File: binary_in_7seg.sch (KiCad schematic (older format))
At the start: 9 parts

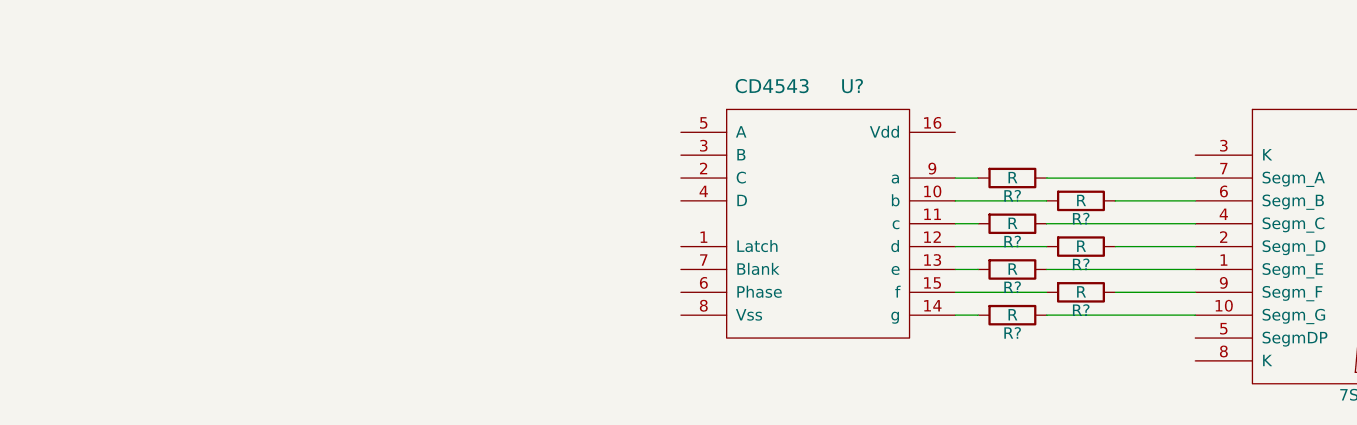
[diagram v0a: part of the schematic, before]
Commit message: Filled in more of the schematic
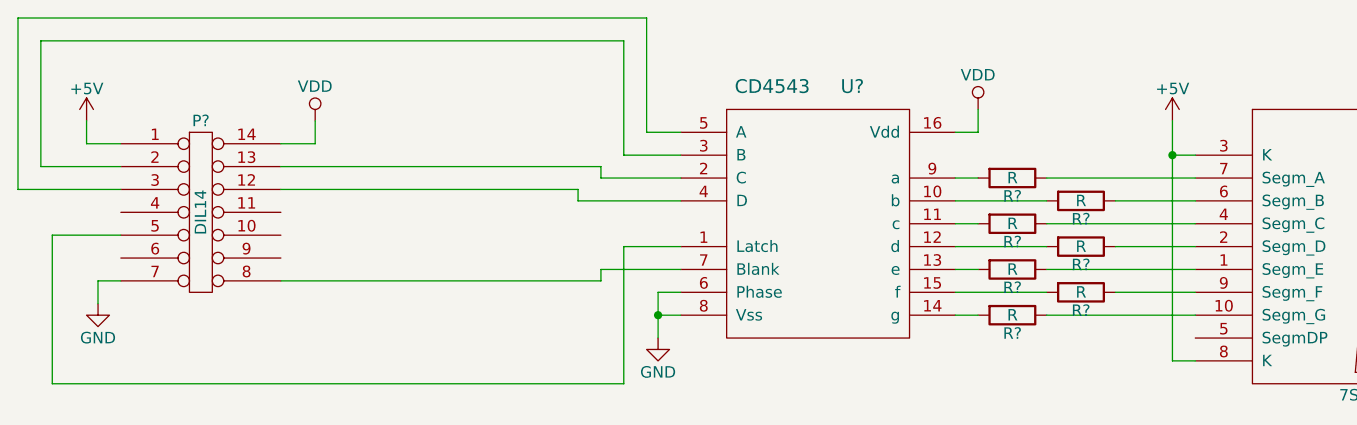
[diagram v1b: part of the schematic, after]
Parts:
- added P?: DIL14, symbol DIL14
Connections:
- net +5V: now reaches S?.3 (K)
- net +5V: now also S?.8 (K), P?.1
- net at U?.1 (Latch): now also P?.5
- net VDD: now reaches U?.16 (Vdd)
- net VDD: now also P?.14
- net at U?.2 (C): now also P?.13
- net at U?.3 (B): now also P?.2
- net at U?.4 (D): now also P?.12
- net at U?.5 (A): now also P?.3
- net GND: now reaches U?.6 (Phase)
- net GND: now also U?.8 (Vss), P?.7
- net at U?.7 (Blank): now also P?.8

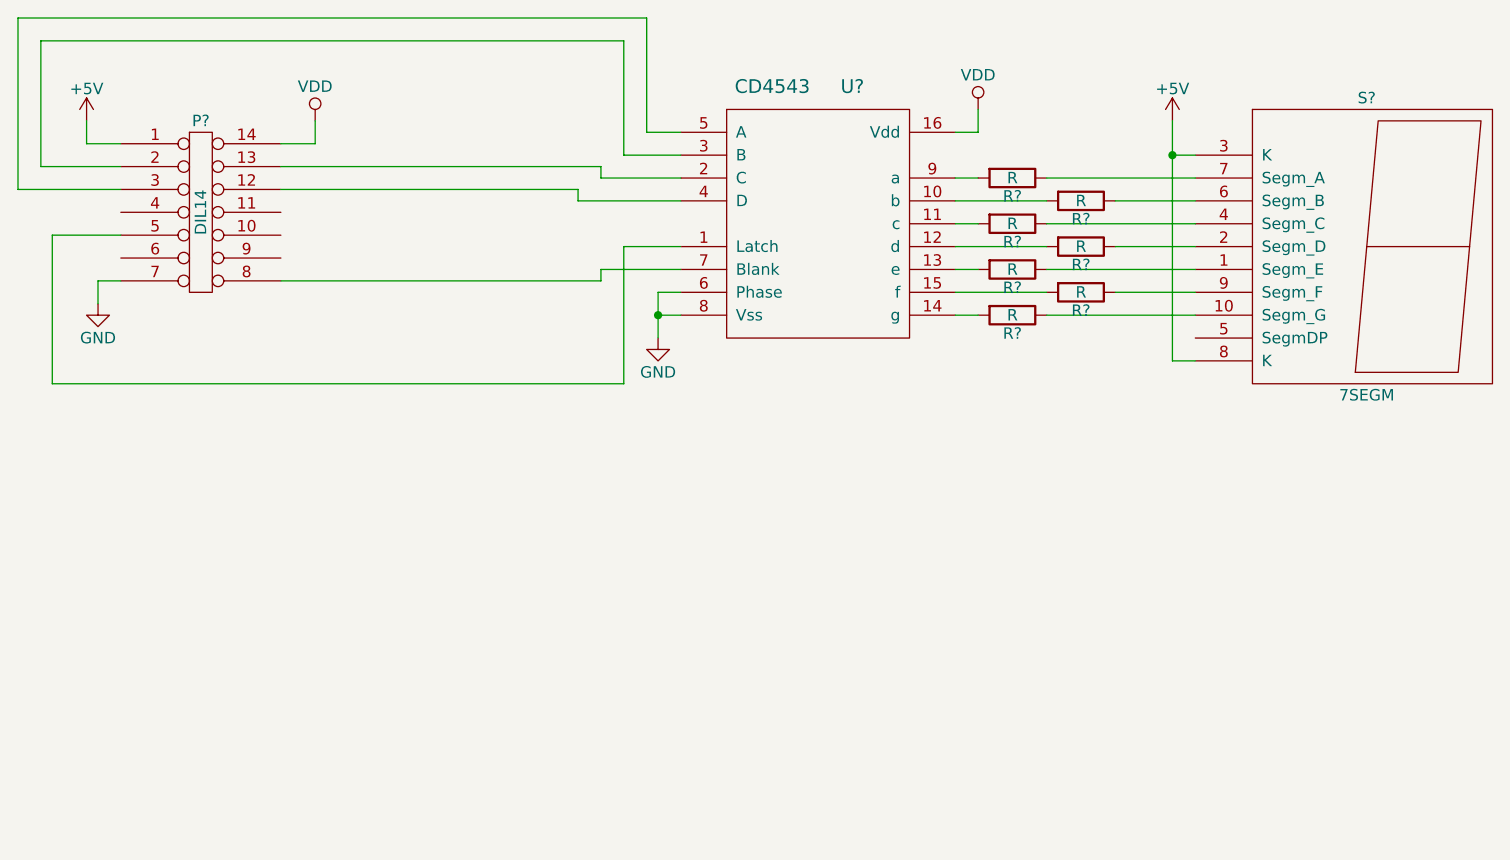
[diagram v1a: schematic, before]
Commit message: Added decimal point input
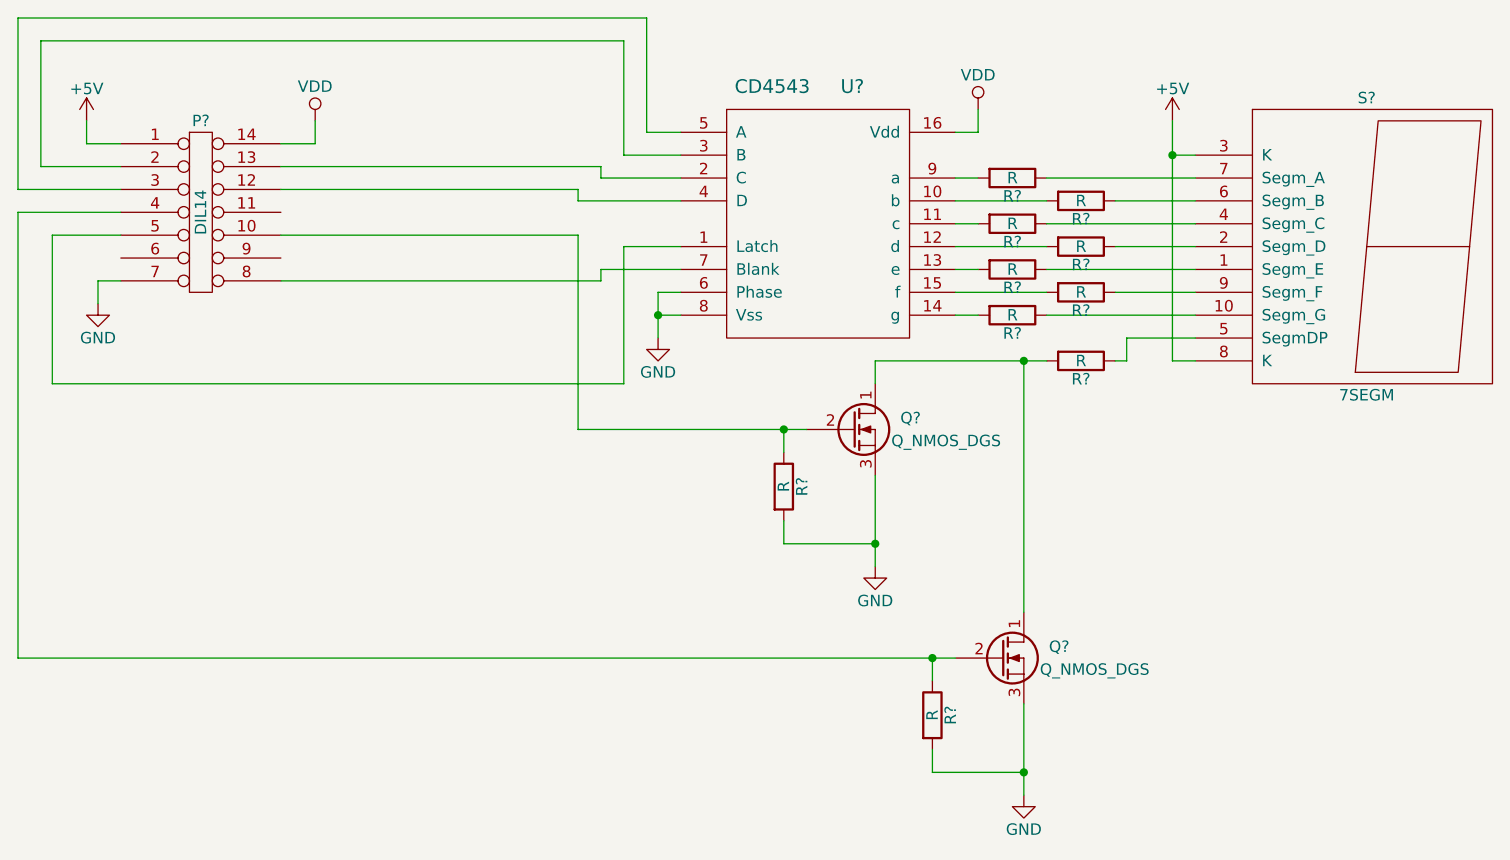
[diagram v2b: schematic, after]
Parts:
- added Q? (x2): Q_NMOS_DGS, symbol Q_NMOS_DGS
- added R? (x3): R, symbol R
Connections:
- net GND: now also Q?.3 (S), Q?.3 (S), R?.2, R?.2
- net at S?.5 (SegmDP): now also R?.1
- net at P?.10: now also Q?.2 (G), R?.1
- net at P?.4: now also Q?.2 (G), R?.1
- new net: Q?.1 (D), Q?.1 (D), R?.2
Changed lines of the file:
@@
 $EndComp
 Wire Wire Line
-	8200 2650 8200 3700
+	8200 2650 8200 2800
+Wire Wire Line
+	8200 2800 8200 3700
 Wire Wire Line
 	8200 2800 8300 2800
@@
 $EndComp
 Wire Wire Line
-	5950 3400 5950 3600
+	5950 3400 5950 3500
+Wire Wire Line
+	5950 3500 5950 3600
 Wire Wire Line
 	5950 3500 6050 3500
@@
 	6050 3400 5950 3400
 Connection ~ 5950 3500
+$Comp
+L Q_NMOS_DGS Q?
+U 1 1 57E026D3
+P 6800 4000
+F 0 "Q?" H 7100 4050 50  0000 R CNN
+F 1 "Q_NMOS_DGS" H 7450 3950 50  0000 R CNN
+F 2 "" H 7000 4100 50  0000 C CNN
+F 3 "" H 6800 4000 50  0000 C CNN
+	1    6800 4000
+	1    0    0    -1
+$EndComp
+$Comp
+L Q_NMOS_DGS Q?
+U 1 1 57E0271C
+P 7450 5000
+F 0 "Q?" H 7750 5050 50  0000 R CNN
+F 1 "Q_NMOS_DGS" H 8100 4950 50  0000 R CNN
+F 2 "" H 7650 5100 50  0000 C CNN
+F 3 "" H 7450 5000 50  0000 C CNN
+	1    7450 5000
+	1    0    0    -1
+$EndComp
+$Comp
+L GND #PWR?
+U 1 1 57E027E1
+P 6900 4600
+F 0 "#PWR?" H 6900 4350 50  0001 C CNN
+F 1 "GND" H 6900 4450 50  0000 C CNN
+F 2 "" H 6900 4600 50  0000 C CNN
+F 3 "" H 6900 4600 50  0000 C CNN
+	1    6900 4600
+	1    0    0    -1
+$EndComp
+$Comp
+L GND #PWR?
+U 1 1 57E0284C
+P 7550 5600
+F 0 "#PWR?" H 7550 5350 50  0001 C CNN
+F 1 "GND" H 7550 5450 50  0000 C CNN
+F 2 "" H 7550 5600 50  0000 C CNN
+F 3 "" H 7550 5600 50  0000 C CNN
+	1    7550 5600
+	1    0    0    -1
+$EndComp
+Wire Wire Line
+	7550 5200 7550 5500
+Wire Wire Line
+	7550 5500 7550 5600
+Wire Wire Line
+	6900 4200 6900 4500
+Wire Wire Line
+	6900 4500 6900 4600
+$Comp
+L R R?
+U 1 1 57E02906
+P 6500 4250
+F 0 "R?" V 6580 4250 50  0000 C CNN
+F 1 "R" V 6500 4250 50  0000 C CNN
+F 2 "" V 6430 4250 50  0000 C CNN
+F 3 "" H 6500 4250 50  0000 C CNN
+	1    6500 4250
+	1    0    0    -1
+$EndComp
+$Comp
+L R R?
+U 1 1 57E02947
+P 7150 5250
+F 0 "R?" V 7230 5250 50  0000 C CNN
+F 1 "R" V 7150 5250 50  0000 C CNN
+F 2 "" V 7080 5250 50  0000 C CNN
+F 3 "" H 7150 5250 50  0000 C CNN
+	1    7150 5250
+	1    0    0    -1
+$EndComp
+Wire Wire Line
+	6500 4100 6500 4000
+Wire Wire Line
+	5600 4000 6500 4000
+Wire Wire Line
+	6500 4000 6600 4000
+Wire Wire Line
+	7150 5100 7150 5000
+Wire Wire Line
+	3150 5000 7150 5000
+Wire Wire Line
+	7150 5000 7250 5000
+Wire Wire Line
+	7150 5400 7150 5500
+Wire Wire Line
+	7150 5500 7550 5500
+Connection ~ 7550 5500
+Wire Wire Line
+	6500 4400 6500 4500
+Wire Wire Line
+	6500 4500 6900 4500
+Connection ~ 6900 4500
+Wire Wire Line
+	4300 3150 5600 3150
+Wire Wire Line
+	5600 3150 5600 4000
+Connection ~ 6500 4000
+Wire Wire Line
+	7550 4800 7550 3700
+Wire Wire Line
+	6900 3700 7550 3700
+Wire Wire Line
+	7550 3700 7650 3700
+Wire Wire Line
+	6900 3700 6900 3800
+Wire Wire Line
+	8000 3700 8000 3600
+Wire Wire Line
+	8000 3600 8300 3600
+Connection ~ 7550 3700
+Wire Wire Line
+	3600 3050 3150 3050
+Wire Wire Line
+	3150 3050 3150 5000
+Connection ~ 7150 5000
+$Comp
+L R R?
+U 1 1 57E0311F
+P 7800 3700
+F 0 "R?" V 7880 3700 50  0000 C CNN
+F 1 "R" V 7800 3700 50  0000 C CNN
+F 2 "" V 7730 3700 50  0000 C CNN
+F 3 "" H 7800 3700 50  0000 C CNN
+	1    7800 3700
+	0    1    1    0
+$EndComp
+Wire Wire Line
+	7950 3700 8000 3700
 $EndSCHEMATC
